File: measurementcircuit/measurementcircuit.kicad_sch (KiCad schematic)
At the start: 166 parts, among them J1 Conn_01x02, J10 Conn_01x02, J11 Conn_01x02, J12 Conn_01x02, J13 2604-3102, J14 DILB28P-223TLF, J15 Conn_01x02, J16 Conn_01x02, J17 Conn_01x02, J18 2604-3102, J19 2604-3102, J2 Conn_01x02, J20 2604-3102, J21 Conn_01x02, J22 Conn_01x02, J23 Conn_01x02, J24 Conn_01x02, J25 Conn_01x02, J26 Conn_01x02, J27 Conn_01x02, J28 Conn_01x02, J29 Conn_01x02, J3 2604-3102, J30 Conn_01x02, J31 Conn_01x02, J32 Conn_01x02, J33 Conn_01x02, J34 Conn_01x02, J35 Conn_01x02, J36 Conn_01x02, J37 Conn_01x02, J38 Conn_01x02, J39 Conn_01x02, J4 2604-3102, J40 Conn_01x02, J41 Conn_01x02, J42 Conn_01x02, J43 DILB28P-223TLF, J44 2601-1102, J45 2601-1108, J46 2601-1108, J47 Conn_01x02, J48 Conn_01x02, J49 Conn_01x02, J5 2604-3102, J50 2604-3102, J51 Conn_01x02, J52 Conn_01x02, J53 Conn_01x02, J54 Conn_01x02, J55 2604-3102, J56 Conn_01x02, J57 Conn_01x02, J58 Conn_01x02, J59 Conn_01x02, J6 2604-3102, J60 2601-1108, J61 2604-3102, J62 Conn_01x02, J63 Conn_01x02, J64 Conn_01x02, J65 Conn_01x02, J66 2604-3102, J67 Conn_01x02, J68 Conn_01x02, J69 Conn_01x02, J7 2604-3102, J70 Conn_01x02, J71 2604-3102, J72 Conn_01x02, J73 Conn_01x02, J74 Conn_01x02, J75 Conn_01x02, J76 2604-3102, J77 Conn_01x02, J78 Conn_01x02, J79 Conn_01x02, J8 Conn_01x02, J80 Conn_01x02, J81 2604-3102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

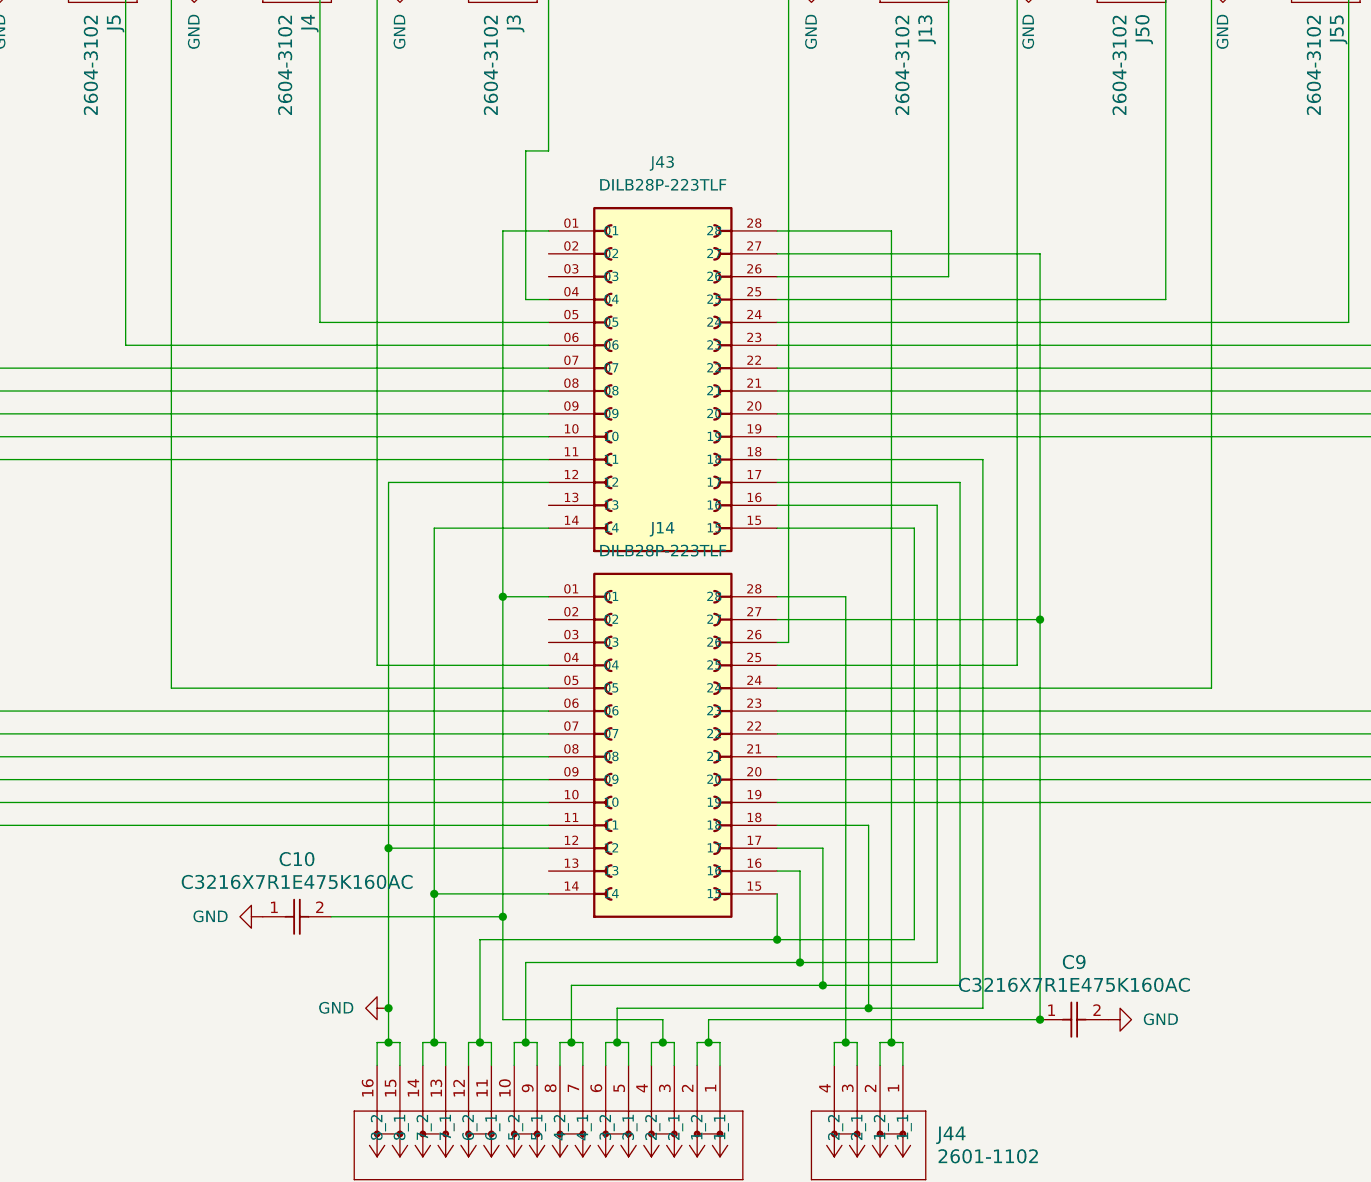
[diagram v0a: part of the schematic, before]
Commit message: Add Decoupling Caps and Local Bulk Caps for VDD and VSS rails
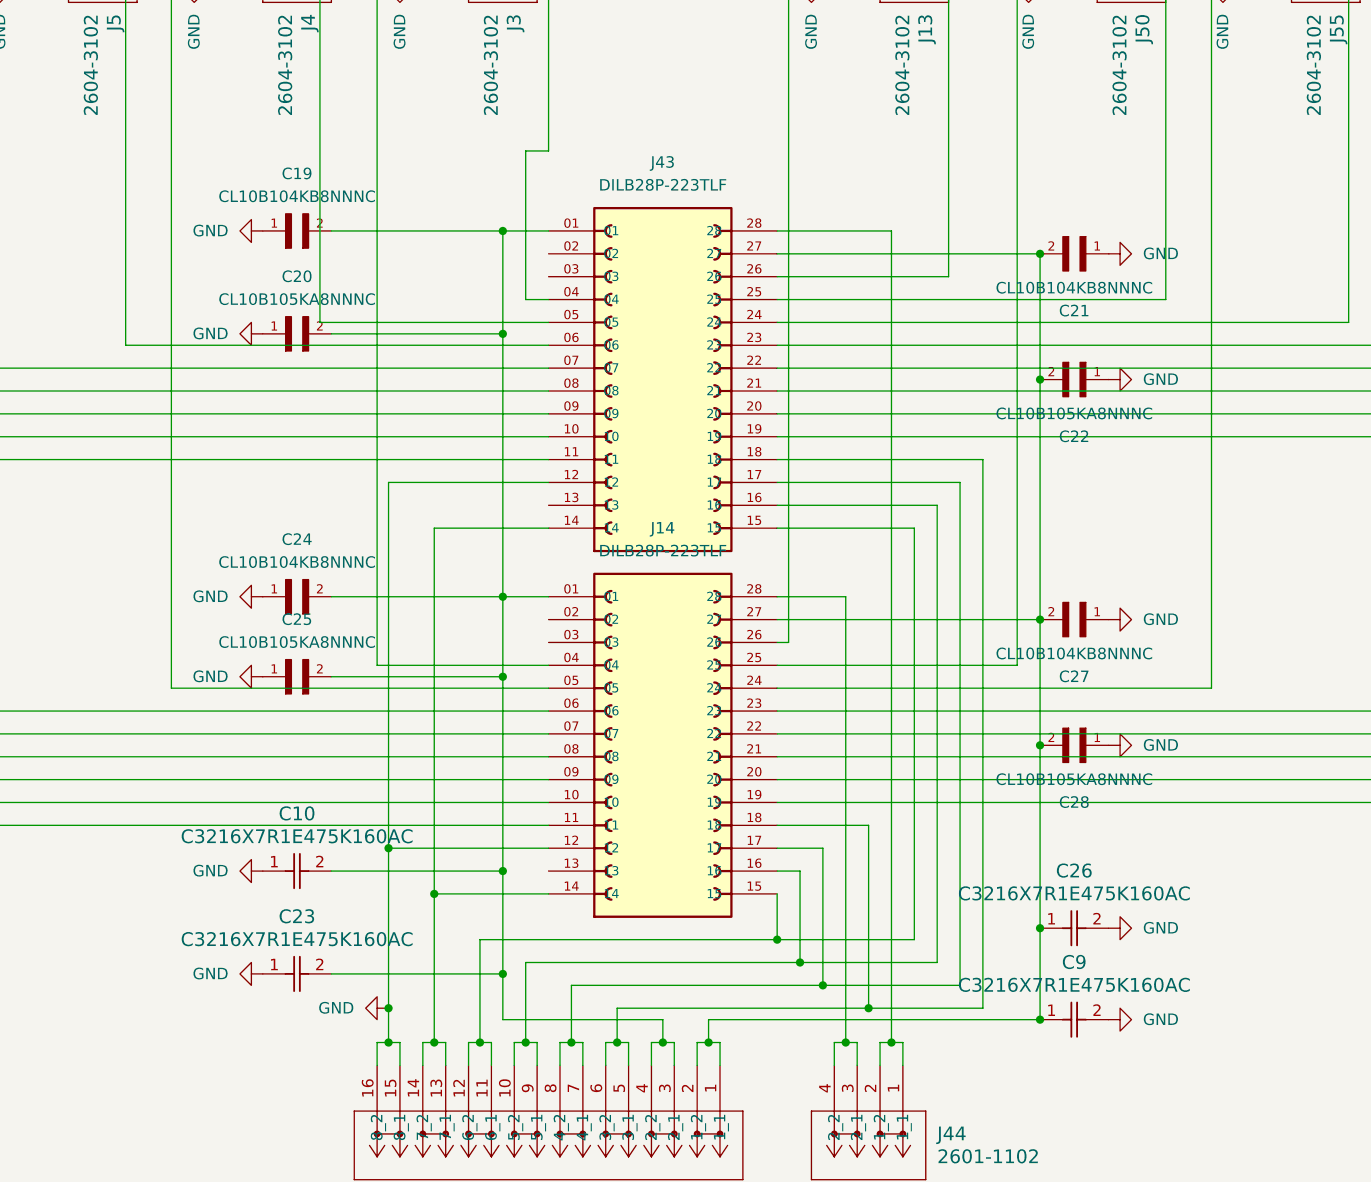
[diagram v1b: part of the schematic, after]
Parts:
- added C19, C21, C24, C27: CL10B104KB8NNNC, CL10B104KB8NNNC:CAPC1608X90N, symbol 0.1uF_Decoupling_Cap_CL10B104KB8NNNC:CL10B104KB8NNNC
- added C20, C22, C25, C28: CL10B105KA8NNNC, CL10B105KA8NNNC:CAPC1608X90N, symbol 1uF_Local_Bulk_Cap_CL10B105KA8NNNC:CL10B105KA8NNNC
- added C23, C26: C3216X7R1E475K160AC, CAP_3216_TDK, symbol Bulk_Cap_2025-12-21_04-50-52:C3216X7R1E475K160AC
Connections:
- net GND: now also C19.1, C20.1, C21.1, C22.1, C23.1, C24.1, C25.1, C26.2, C27.1, C28.1
- net at C10.2, J14.01, J43.01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: now also C19.2, C20.2, C23.2, C24.2, C25.2
- net at C9.1, J14.27, J43.27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: now also C21.2, C22.2, C26.1, C27.2, C28.2
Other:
- moved on the sheet: C10

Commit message: Add footprints, reassign footprints, change power supply connectors to new 2-pole style
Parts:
- C10, C23, C26, C9: footprint CAP_3216_TDK -> 4.7uF_Bulk_Cap:CAP_3216_TDK
- C11, C12, C13, C14, C15, C16, C18, C2, C3, C4, C5, C6, C7, C8: footprint Capacitor_SMD:C_0805_2012Metric -> 10pF_Capacitor_Custom:C_Disc_Radial_P5.90mm_W4.3mm_L11.4mm_Placeholder
- C19, C21, C24, C27: footprint CL10B104KB8NNNC:CAPC1608X90N -> 0.1uF_Decoup_Cap:CAPC1608X90N
- C20, C22, C25, C28: footprint CL10B105KA8NNNC:CAPC1608X90N -> 1uF_Local_Bulk_Cap:CAPC1608X90N
- J13, J18, J19, J20, J3, J4, J5, J50, J55, J6, J61, J66, J7, J71, J76, J81: footprint Wago - 2604-3302_2_pole_connector:CONN2_2604-3302_WAG -> CONN2_2601-1102_WAG; symbol CONN2:2604-3102 -> 2_Pole_Terminal_Block_2025-12-21_05-29-27:2601-1102
- J14, J43: footprint DILB28P-223TLF:AMPHENOL_DILB28P-223TLF -> DIP socket DILB28P_223TLF:AMPHENOL_DILB28P-223TLF
- J44: footprint CONN2_2601-1102_WAG -> 2_pole_term_block:CONN2_2601-1102_WAG
- J45, J46, J60: footprint CONN8_2601-1108_WAG -> 8_Pole_Terminal_Block:CONN8_2601-1108_WAG
- L1, L10, L11, L12, L13, L14, L15, L16, L2, L3, L4, L5, L6, L7, L8, L9: footprint Inductor_SMD:L_0805_2012Metric -> 56uH_Inductor:INDAD1400W80L920D650
- R1, R10, R13, R16, R19, R22, R25, R28, R31, R34, R37, R4, R40, R43, R46, R7: footprint Resistor_THT:R_Axial_Power_L38.0mm_W9.0mm_P40.64mm -> 10Ohm Resistor:RS010_VIS
- R11, R14, R17, R2, R20, R23, R26, R29, R32, R35, R38, R41, R44, R47, R5, R8: footprint Resistor_THT:R_Axial_Power_L20.0mm_W6.4mm_P25.40mm -> 50Ohm_R:RES_CMF60_VIS
- R12, R15, R18, R21, R24, R27, R3, R30, R33, R36, R39, R42, R45, R48, R6, R9: footprint Resistor_THT:R_Axial_DIN0309_L9.0mm_D3.2mm_P5.08mm_Vertical -> 500Ohm_R:CMF65_VIS
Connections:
- net at C1.1, J43.05, L2.2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: no longer J14.05, J4.1 (1_1), J4.2 (1_2), J9.2 (Pin_2)
- net at J22.1 (Pin_1), J23.1 (Pin_1), J24.1 (Pin_1)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: now also J14.05, J4.1 (1_1), J4.2 (1_2), J9.2 (Pin_2)

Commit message: Major PCB work, Ready for review
Still need to reassign 3D models
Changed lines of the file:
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@@
 		(dnp no)
 		(property "Reference" "J70"
-			(at 358.1399 102.87 0)
+			(at 364.236 107.188 0)
 			(effects
 				(font
